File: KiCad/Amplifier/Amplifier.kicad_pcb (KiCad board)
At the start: 2 copper layers, 48 x 53 mm, 29 parts, among them J1 Screw_Terminal_01x03, J2 Screw_Terminal_01x03, Q1 NPN, Q2 NPN, U1 TL074

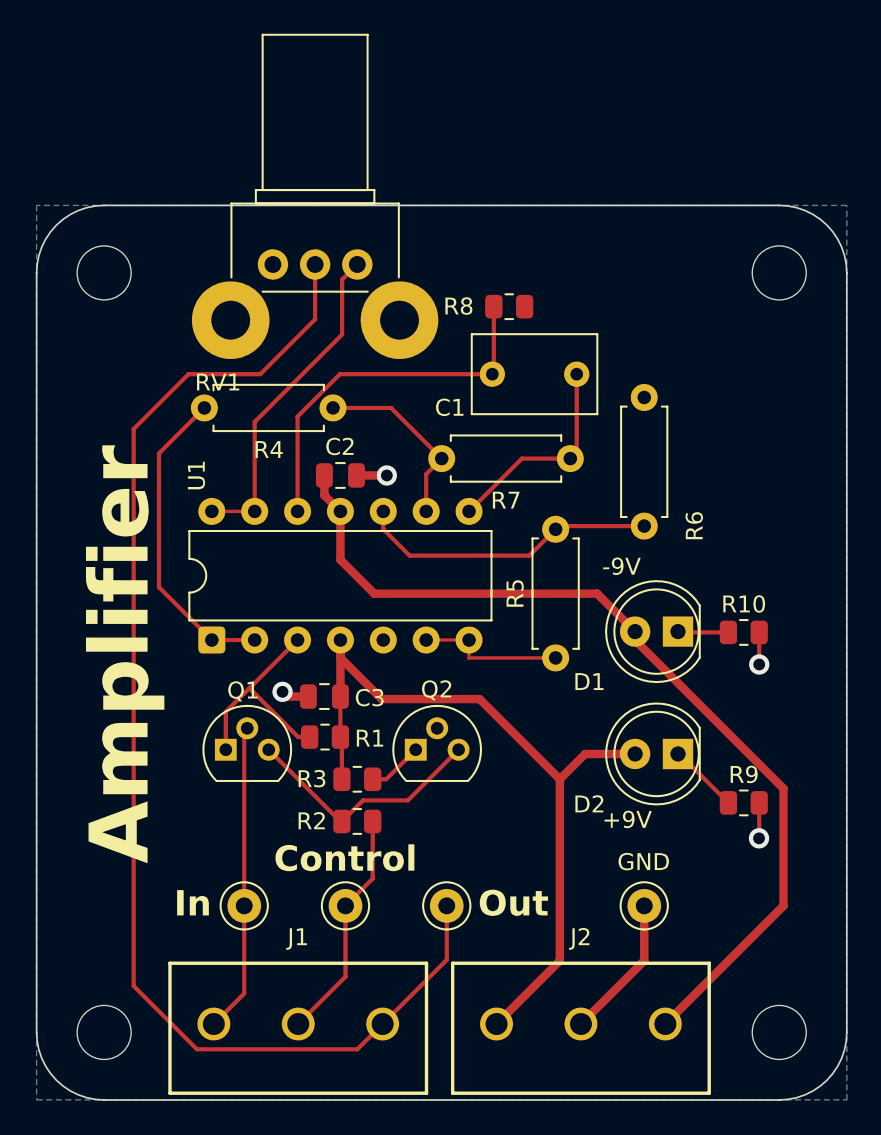
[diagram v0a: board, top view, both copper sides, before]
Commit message: added silkscreen to help assembly process on all boards
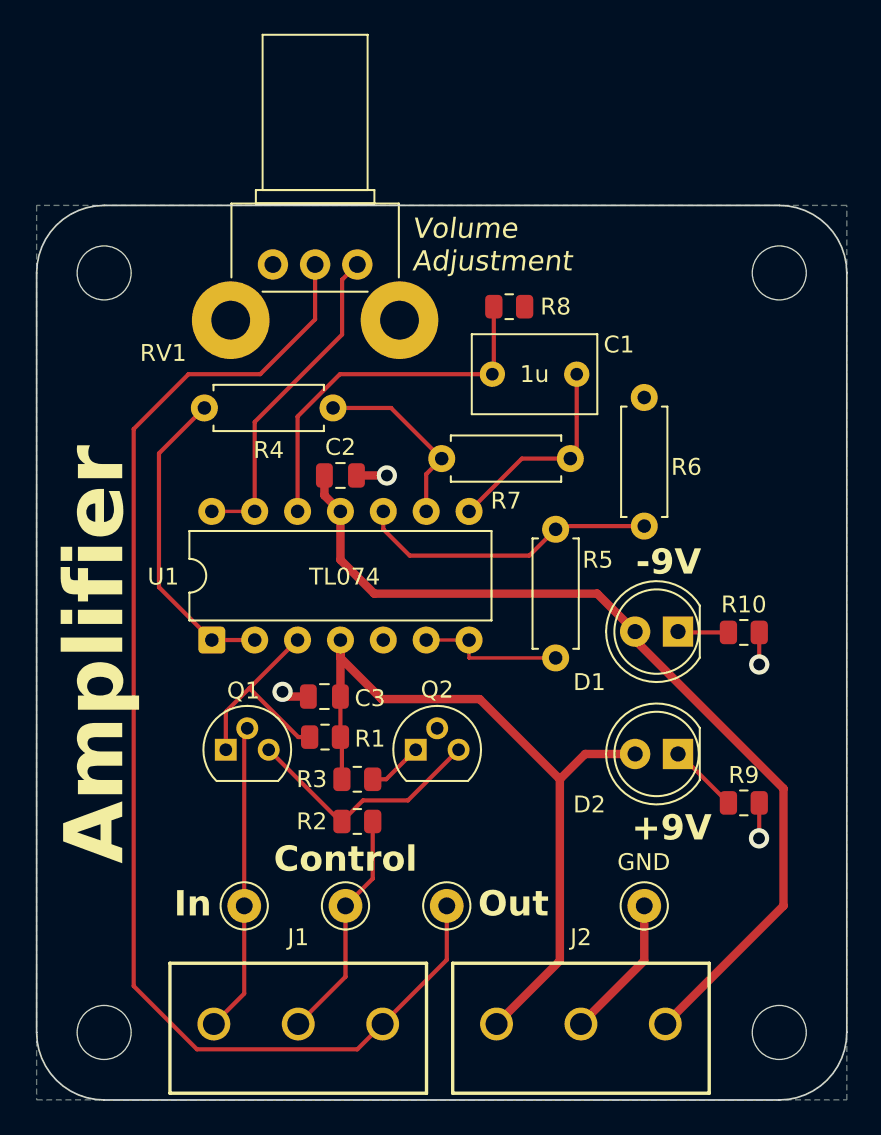
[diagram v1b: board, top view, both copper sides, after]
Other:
- board text added: "Volume Adjustment"
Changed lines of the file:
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@@
 		(tags "THT DIP DIL PDIP 2.54mm 7.62mm 300mil")
 		(property "Reference" "U1"
-			(at 9.75 -0.88 90)
+			(at 3.75 -2.88 180)
 			(layer "F.SilkS")
 			(effects
@@
 		)
 		(property "Value" "TL074"
-			(at 3.81 17.57 90)
-			(layer "F.Fab")
+			(at 3.75 7.87 180)
+			(layer "F.SilkS")
 			(effects
 				(font
@@
 		(tags "Resistor Axial_DIN0207 series Axial Horizontal pin pitch 7.62mm 0.25W = 1/4W length 6.3mm diameter 2.5mm")
 		(property "Reference" "R5"
-			(at 3.81 -2.37 90)
+			(at 5.81 2.5 180)
 			(layer "F.SilkS")
 			(effects
@@
 		(tags "Potentiometer horizontal Bourns PTV09A-2 Single")
 		(property "Reference" "RV1"
-			(at -7 -8.25 180)
+			(at -5.25 -11.5 180)
 			(layer "F.SilkS")
 			(effects
@@
 		(tags "C Rect series Radial pin pitch 5.00mm length 7.2mm width 4.5mm Capacitor R82")
 		(property "Reference" "C1"
-			(at 7.5 -2 0)
+			(at -2.5 1.75 0)
 			(layer "F.SilkS")
 			(effects
@@
 		)
 		(property "Value" "1u"
-			(at 2.5 3.5 0)
-			(layer "F.Fab")
+			(at 2.5 0 0)
+			(layer "F.SilkS")
 			(effects
 				(font
@@
 		(tags "Resistor Axial_DIN0207 series Axial Horizontal pin pitch 7.62mm 0.25W = 1/4W length 6.3mm diameter 2.5mm")
 		(property "Reference" "R6"
-			(at 0 3 90)
+			(at 3.5 2.5 180)
 			(layer "F.SilkS")
 			(effects
@@
 		(tags "resistor")
 		(property "Reference" "R8"
-			(at -3 0 0)
+			(at 2.75 0 0)
 			(layer "F.SilkS")
 			(effects
@@
 		(layer "Edge.Cuts")
 	)
-	(gr_text "-9V"
-		(at 75.5 57 0)
+	(gr_text "GND"
+		(at 76.4 74.5 0)
 		(layer "F.SilkS")
 		(effects
@@
 		)
 	)
-	(gr_text "+9V"
-		(at 75.5 72 0)
+	(gr_text "Volume\nAdjustment"
+		(at 64.25 39 0)
 		(layer "F.SilkS")
 		(effects
 			(font
-				(size 1 1)
+				(size 1.2 1.2)
 				(thickness 0.15)
+				(italic yes)
 			)
 			(justify left bottom)
 		)
 	)
-	(gr_text "GND"
-		(at 76.4 74.5 0)
+	(gr_text "+9V"
+		(at 77.25 72.75 0)
 		(layer "F.SilkS")
 		(effects
 			(font
-				(size 1 1)
-				(thickness 0.15)
+				(size 1.5 1.5)
+				(thickness 0.3)
+				(bold yes)
+			)
+			(justify left bottom)
+		)
+	)
+	(gr_text "-9V"
+		(at 77.5 57 0)
+		(layer "F.SilkS")
+		(effects
+			(font
+				(size 1.5 1.5)
+				(thickness 0.3)
+				(bold yes)
 			)
 			(justify left bottom)
@@
 	)
 	(gr_text "Amplifier"
-		(at 49 74 90)
+		(at 47.5 74 90)
 		(layer "F.SilkS")
 		(effects

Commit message: ran DRC on all boards
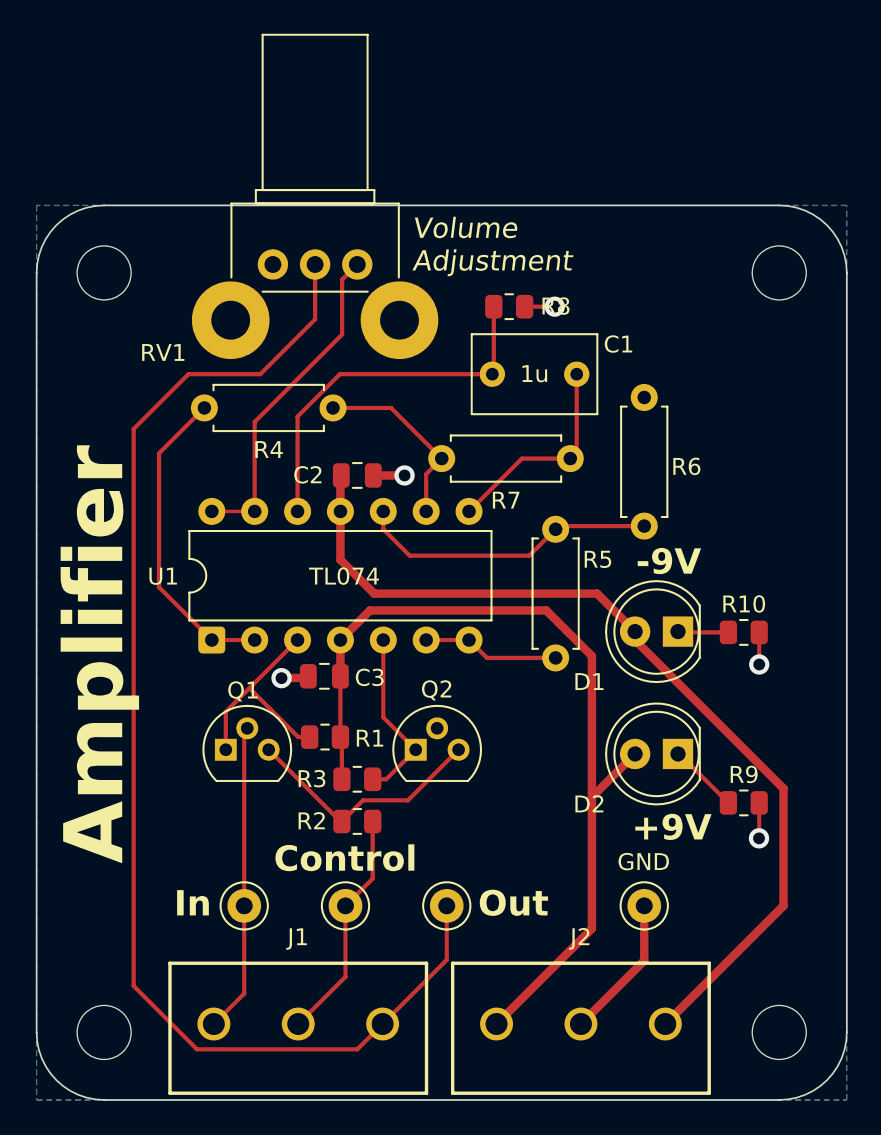
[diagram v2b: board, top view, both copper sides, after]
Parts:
- moved C3 1.20 mm to (59.0, 62.9)
- moved C2 1.00 mm to (61.0, 51.0)
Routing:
- net Net-(Q2-C): track 3.27 -> 10.6 mm
- net +9V: track 46.5 -> 52.8 mm
- net GND: track 16.0 -> 17.8 mm, vias 4 -> 5
- net Net-(U1B--): track 8.73 -> 8.11 mm
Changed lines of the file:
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@@
 	(footprint "Capacitor_SMD:C_0805_2012Metric"
 		(layer "F.Cu")
-		(at 59.05 64.1)
+		(at 59.05 62.9)
 		(descr "Capacitor SMD 0805 (2012 Metric), square (rectangular) end terminal, IPC-7351 nominal, (Body size source: IPC-SM-782 page 76, https://www.pcb-3d.com/wordpress/wp-content/uploads/ipc-sm-782a_amendment_1_and_2.pdf, https://docs.google.com/spreadsheets/d/1BsfQQcO9C6DZCsRaXUlFlo91Tg2WpOkGARC1WS5S8t0/edit?usp=sharing)")
 		(tags "capacitor")
@@
 	(footprint "Capacitor_SMD:C_0805_2012Metric"
 		(layer "F.Cu")
-		(at 60 51)
+		(at 61 51)
 		(descr "Capacitor SMD 0805 (2012 Metric), square (rectangular) end terminal, IPC-7351 nominal, (Body size source: IPC-SM-782 page 76, https://www.pcb-3d.com/wordpress/wp-content/uploads/ipc-sm-782a_amendment_1_and_2.pdf, https://docs.google.com/spreadsheets/d/1BsfQQcO9C6DZCsRaXUlFlo91Tg2WpOkGARC1WS5S8t0/edit?usp=sharing)")
 		(tags "capacitor")
 		(property "Reference" "C2"
-			(at 0 -1.68 0)
+			(at -2.9 0 0)
 			(layer "F.SilkS")
 			(effects
@@
 	)
 	(segment
-		(start 60.0875 66.5875)
-		(end 60 66.5)
-		(width 0.25)
+		(start 72.2 59)
+		(end 61.75 59)
+		(width 0.5)
 		(layer "F.Cu")
 		(net "+9V")
 	)
 	(segment
-		(start 62.445 64.25)
-		(end 60 61.805)
+		(start 60 60.75)
+		(end 60 62.9)
 		(width 0.5)
 		(layer "F.Cu")
@@
 	)
 	(segment
-		(start 60 66.5)
-		(end 60 64.1)
-		(width 0.25)
+		(start 74.9 61.7)
+		(end 72.2 59)
+		(width 0.5)
 		(layer "F.Cu")
 		(net "+9V")
 	)
 	(segment
-		(start 73 79.75)
-		(end 73 69)
+		(start 69.25 83.5)
+		(end 74.9 77.85)
 		(width 0.5)
 		(layer "F.Cu")
@@
 	)
 	(segment
-		(start 60 61.805)
-		(end 60 60.75)
-		(width 0.5)
+		(start 60.0875 66.5875)
+		(end 60 66.5)
+		(width 0.25)
 		(layer "F.Cu")
 		(net "+9V")
 	)
 	(segment
-		(start 69.25 83.5)
-		(end 73 79.75)
+		(start 74.9 70.06)
+		(end 77.46 67.5)
 		(width 0.5)
 		(layer "F.Cu")
@@
 	)
 	(segment
-		(start 68.25 64.25)
-		(end 62.445 64.25)
+		(start 61.75 59)
+		(end 60 60.75)
 		(width 0.5)
 		(layer "F.Cu")
@@
 	)
 	(segment
-		(start 73 69)
-		(end 74.5 67.5)
+		(start 74.9 70.06)
+		(end 74.9 61.7)
 		(width 0.5)
 		(layer "F.Cu")
@@
 	)
 	(segment
-		(start 74.5 67.5)
-		(end 77.46 67.5)
+		(start 74.9 77.85)
+		(end 74.9 70.06)
 		(width 0.5)
 		(layer "F.Cu")
@@
 	)
 	(segment
-		(start 60 60.75)
-		(end 60 64.1)
-		(width 0.5)
+		(start 60 66.5)
+		(end 60 62.9)
+		(width 0.25)
 		(layer "F.Cu")
 		(net "+9V")
 	)
 	(segment
-		(start 73 69)
-		(end 68.25 64.25)
-		(width 0.5)
+		(start 62.54 60.75)
+		(end 62.54 65.33)
+		(width 0.25)
 		(layer "F.Cu")
-		(net "+9V")
+		(net "Net-(Q2-C)")
 	)
 	(segment
@@
 	)
 	(segment
+		(start 62.54 65.33)
+		(end 64.46 67.25)
+		(width 0.25)
+		(layer "F.Cu")
+		(net "Net-(Q2-C)")
+	)
+	(segment
 		(start 61.9125 69)
 		(end 62.71 69)
@@
 		(start 65.08 60.75)
 		(end 67.62 60.75)
-		(width 0.2)
-		(layer "F.Cu")
-		(net "Net-(U1B--)")
-	)
-	(segment
-		(start 72.75 61.81)
-		(end 67.625 61.81)
-		(width 0.2)
+		(width 0.25)
 		(layer "F.Cu")
 		(net "Net-(U1B--)")
 	)
 	(segment
-		(start 67.625 61.81)
-		(end 67.62 61.805)
-		(width 0.2)
+		(start 68.68 61.81)
+		(end 67.62 60.75)
+		(width 0.25)
 		(layer "F.Cu")
 		(net "Net-(U1B--)")
 	)
 	(segment
-		(start 67.62 61.805)
-		(end 67.62 60.75)
-		(width 0.2)
+		(start 72.75 61.81)
+		(end 68.68 61.81)
+		(width 0.25)
 		(layer "F.Cu")
 		(net "Net-(U1B--)")
@@
 	)
 	(segment
+		(start 60.05 51)
+		(end 60 51.05)
+		(width 0.5)
+		(layer "F.Cu")
+		(net "-9V")
+	)
+	(segment
 		(start 77.46 60.25)
 		(end 75.21 58)
@@
 	)
 	(segment
-		(start 59.05 51)
-		(end 59.05 52.18)
+		(start 86.25 69.55)
+		(end 77.5 60.8)
 		(width 0.5)
 		(layer "F.Cu")
@@
 	)
 	(segment
-		(start 59.05 52.18)
+		(start 60 51.05)
 		(end 60 53.13)
 		(width 0.5)
@@
 	)
 	(segment
-		(start 86.25 69.55)
-		(end 77.5 60.8)
-		(width 0.5)
-		(layer "F.Cu")
-		(net "-9V")
-	)
-	(segment
 		(start 86.25 76.5)
 		(end 86.25 69.55)
@@
 	)
 	(segment
+		(start 61.95 51)
+		(end 63.8 51)
+		(width 0.5)
+		(layer "F.Cu")
+		(net "GND")
+	)
+	(segment
 		(start 84.8125 72.4875)
 		(end 84.8 72.5)
@@
 	)
 	(segment
-		(start 60.95 51)
-		(end 62.75 51)
+		(start 56.509074 63.009074)
+		(end 56.518148 63)
 		(width 0.5)
 		(layer "F.Cu")
@@
 	)
 	(segment
-		(start 56.85 64.1)
-		(end 58.1 64.1)
+		(start 56.518148 63)
+		(end 58 63)
 		(width 0.5)
 		(layer "F.Cu")
@@
 	)
 	(segment
-		(start 56.569645 63.819645)
-		(end 56.85 64.1)
+		(start 58 63)
+		(end 58.1 62.9)
 		(width 0.5)
 		(layer "F.Cu")
@@
 	)
 	(segment
+		(start 70.9125 41)
+		(end 72.7 41)
+		(width 0.25)
+		(layer "F.Cu")
+		(net "GND")
+	)
+	(segment
 		(start 84.8125 62.2)
 		(end 84.8125 60.3)
@@
 	)
 	(via
-		(at 62.75 51)
+		(at 63.8 51)
 		(size 1.2)
 		(drill 0.7)
@@
 	)
 	(via
-		(at 56.569645 63.819645)
+		(at 56.509074 63.009074)
+		(size 1.2)
+		(drill 0.7)
+		(layers "F.Cu" "B.Cu")
+		(net "GND")
+	)
+	(via
+		(at 72.7 41)
 		(size 1.2)
 		(drill 0.7)

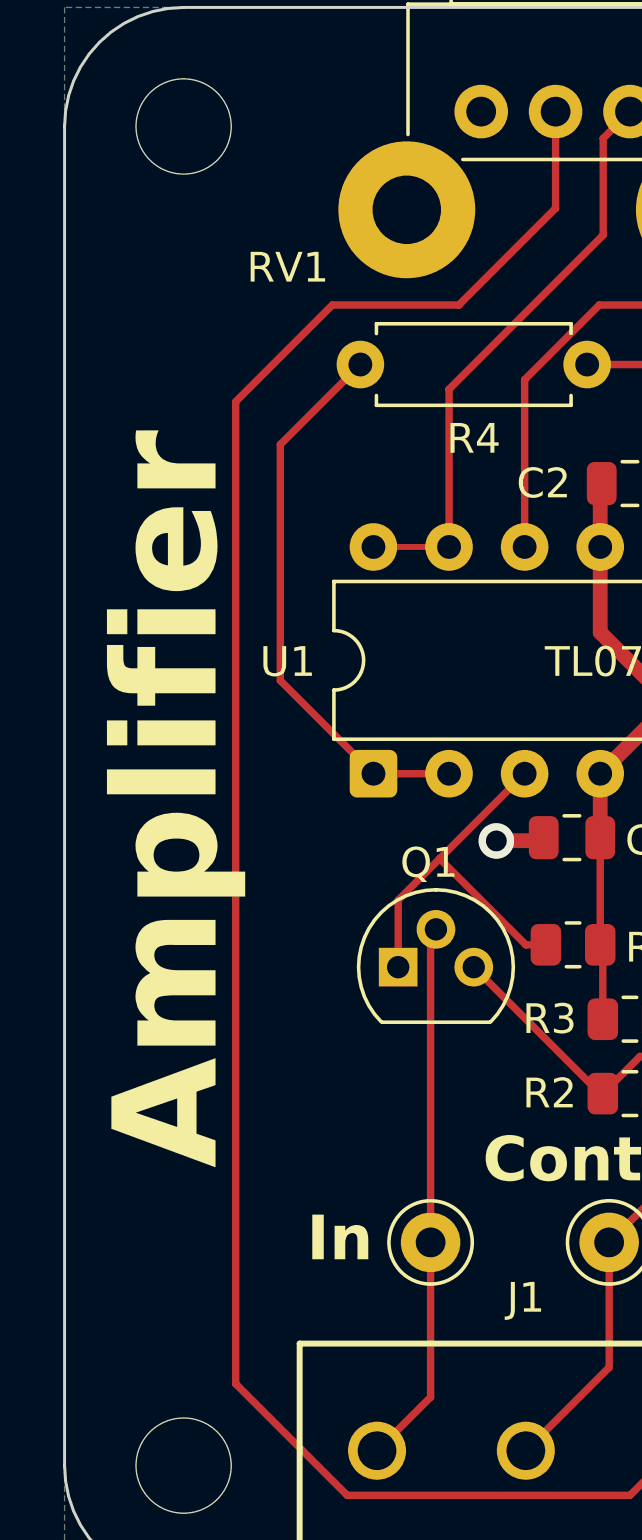
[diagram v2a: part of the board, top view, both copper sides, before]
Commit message: added graphics to some boards
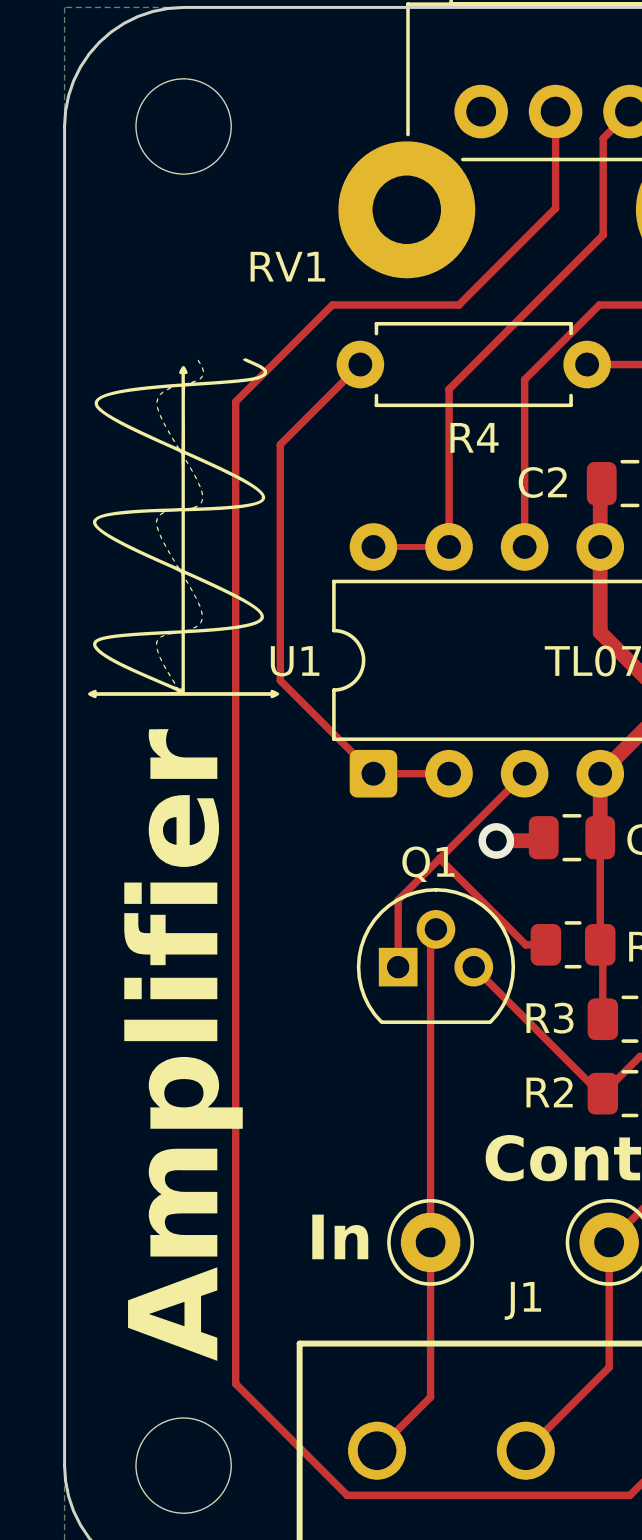
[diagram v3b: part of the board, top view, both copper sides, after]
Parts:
- added G***: LOGO, LOGO, F.Cu at (45.9, 51.1)
